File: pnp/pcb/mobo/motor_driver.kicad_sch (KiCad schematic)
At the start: 34 parts, among them M9 Stepper_Motor, U6 TMC2226-SA

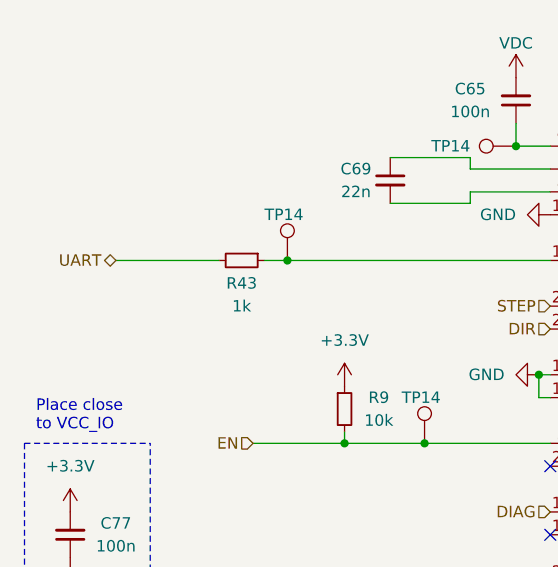
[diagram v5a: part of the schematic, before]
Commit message: Add notes to pending symbols
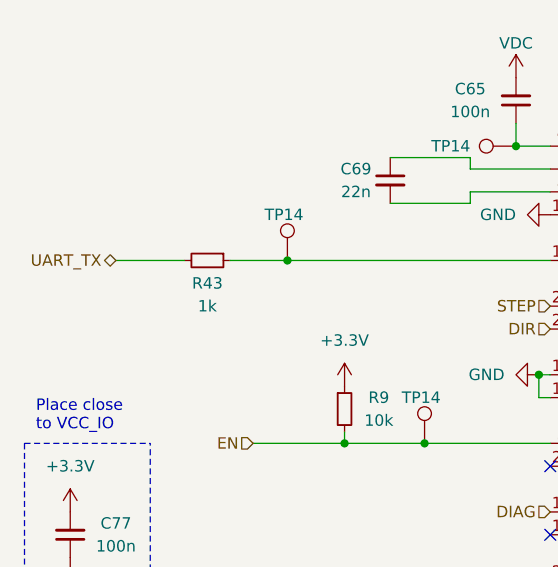
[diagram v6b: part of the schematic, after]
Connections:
- net UART renamed UART_TX
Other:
- moved on the sheet: R43
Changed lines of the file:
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@@
     (stroke (width 0) (type default))
   )
-  (wire (pts (xy 49.53 55.88) (xy 52.07 55.88))
+  (wire (pts (xy 45.72 55.88) (xy 52.07 55.88))
     (stroke (width 0) (type default))
   )
@@
     (stroke (width 0) (type default))
   )
-  (wire (pts (xy 33.02 55.88) (xy 44.45 55.88))
+  (wire (pts (xy 33.02 55.88) (xy 40.64 55.88))
     (stroke (width 0) (type default))
   )
@@
     (effects (font (size 1.27 1.27)) (justify right))
   )
-  (hierarchical_label "UART" (shape bidirectional) (at 33.02 55.88 180) (fields_autoplaced)
+  (hierarchical_label "UART_TX" (shape bidirectional) (at 33.02 55.88 180) (fields_autoplaced)
     (effects (font (size 1.27 1.27)) (justify right))
   )
@@
     )
   )
-  (symbol (lib_id "Device:R_Small") (at 46.99 55.88 270) (unit 1)
-    (in_bom yes) (on_board yes) (dnp no)
-    (property "Reference" "R43" (at 46.99 58.42 90)
-      (effects (font (size 1.27 1.27)))
-    )
-    (property "Value" "1k" (at 46.99 60.96 90)
-      (effects (font (size 1.27 1.27)))
-    )
-    (property "Footprint" "Resistor_SMD:R_0805_2012Metric" (at 46.99 54.102 90)
-      (effects (font (size 1.27 1.27)) hide)
-    )
-    (property "Datasheet" "" (at 46.99 55.88 0)
-      (effects (font (size 1.27 1.27)) hide)
-    )
-    (property "Digikey" "" (at 46.99 55.88 0)
-      (effects (font (size 1.27 1.27)) hide)
-    )
-    (property "JLCPCB" "C17513" (at 46.99 55.88 0)
-      (effects (font (size 1.27 1.27)) hide)
-    )
-    (property "LCSC" "C17513" (at 46.99 55.88 0)
-      (effects (font (size 1.27 1.27)) hide)
-    )
-    (property "Mouser" "" (at 46.99 55.88 0)
-      (effects (font (size 1.27 1.27)) hide)
-    )
-    (property "Notes" "" (at 46.99 55.88 0)
-      (effects (font (size 1.27 1.27)) hide)
-    )
+  (symbol (lib_id "Device:R_Small") (at 43.18 55.88 270) (unit 1)
+    (in_bom yes) (on_board yes) (dnp no)
+    (property "Reference" "R43" (at 43.18 58.42 90)
+      (effects (font (size 1.27 1.27)))
+    )
+    (property "Value" "1k" (at 43.18 60.96 90)
+      (effects (font (size 1.27 1.27)))
+    )
+    (property "Footprint" "Resistor_SMD:R_0805_2012Metric" (at 43.18 54.102 90)
+      (effects (font (size 1.27 1.27)) hide)
+    )
+    (property "Datasheet" "" (at 43.18 55.88 0)
+      (effects (font (size 1.27 1.27)) hide)
+    )
+    (property "Digikey" "" (at 43.18 55.88 0)
+      (effects (font (size 1.27 1.27)) hide)
+    )
+    (property "JLCPCB" "C17513" (at 43.18 55.88 0)
+      (effects (font (size 1.27 1.27)) hide)
+    )
+    (property "LCSC" "C17513" (at 43.18 55.88 0)
+      (effects (font (size 1.27 1.27)) hide)
+    )
+    (property "Mouser" "" (at 43.18 55.88 0)
+      (effects (font (size 1.27 1.27)) hide)
+    )
+    (property "Notes" "" (at 43.18 55.88 0)
+      (effects (font (size 1.27 1.27)) hide)
+    )

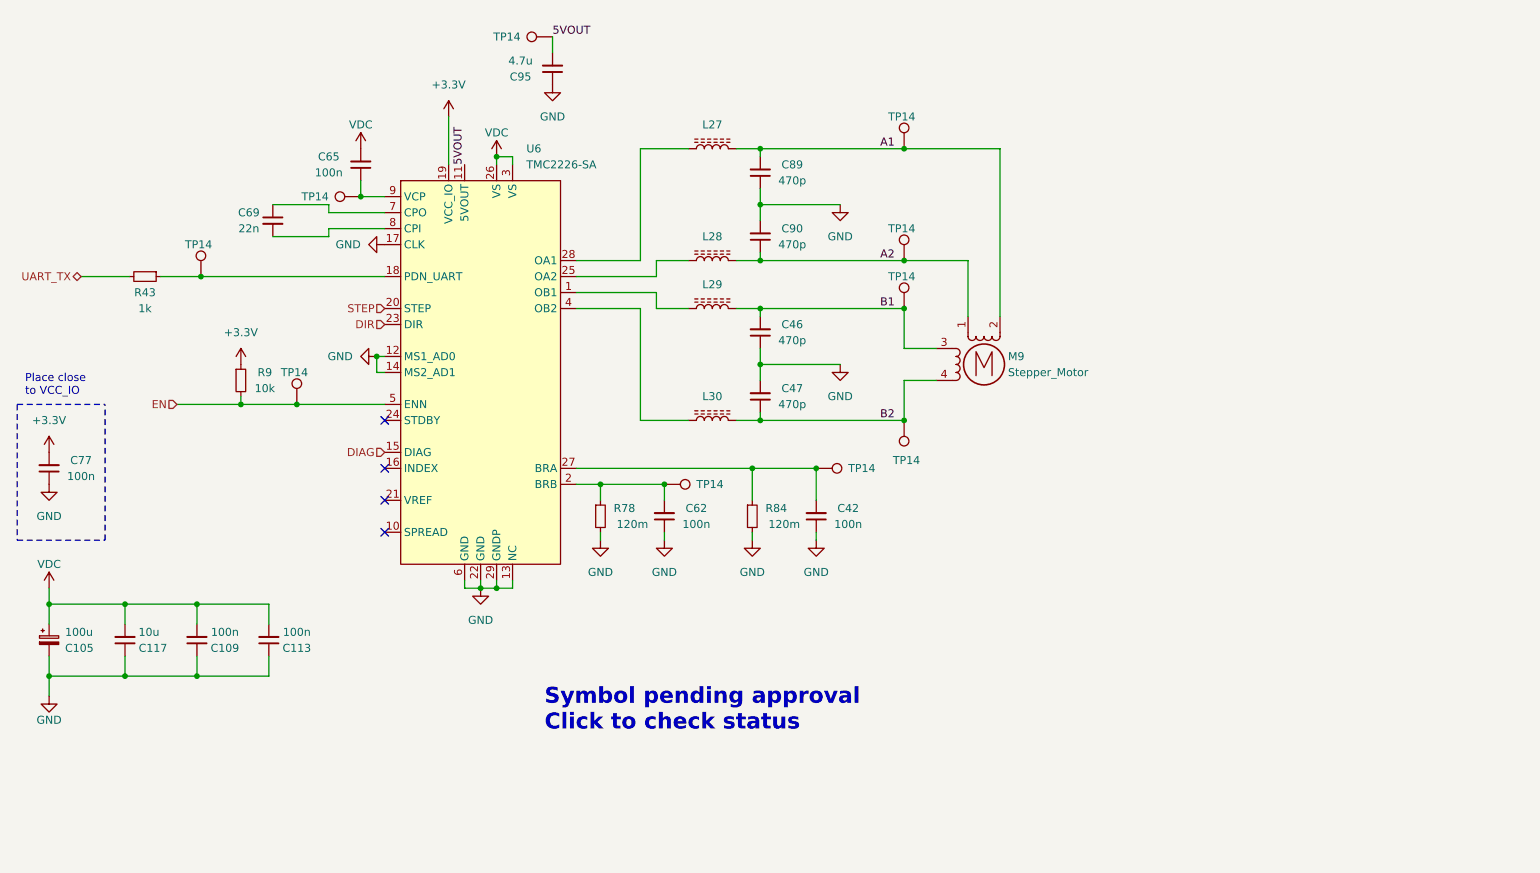
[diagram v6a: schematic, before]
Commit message: Schematic almost finished
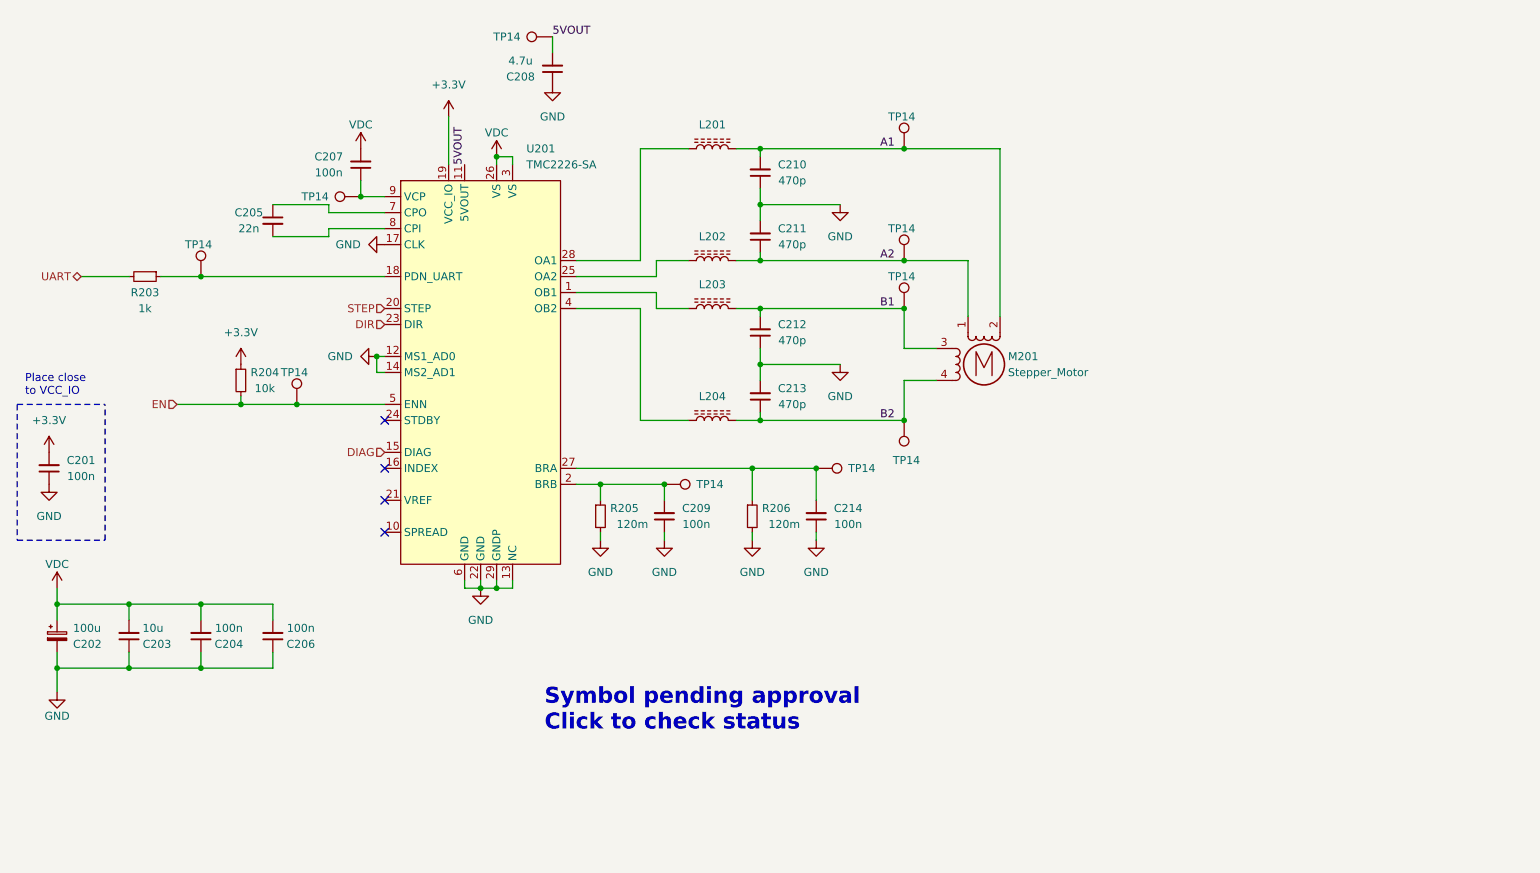
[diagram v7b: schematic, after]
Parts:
- U201: renamed from U6; footprint Package_SO:HTSSOP-28-1EP_4.4x9.7mm_P0.65mm_EP2.75x6.2mm_ThermalVias -> index:HTSSOP-28-1EP_4.4x9.7mm_P0.65mm_EP2.75x6.2mm_ThermalVias
- renumbered C77 to C201, C105 to C202, C117 to C203, C109 to C204, C69 to C205, C113 to C206, C65 to C207, C95 to C208, C62 to C209, C89 to C210, C90 to C211, C46 to C212, C47 to C213, C42 to C214, L27 to L201, L28 to L202, L29 to L203, L30 to L204, M9 to M201, R43 to R203, R9 to R204, R78 to R205, R84 to R206
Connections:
- net UART_TX renamed UART
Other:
- moved on the sheet: C202, C203, C204, C206

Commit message: Finished reverse polarity and inrush current circuits
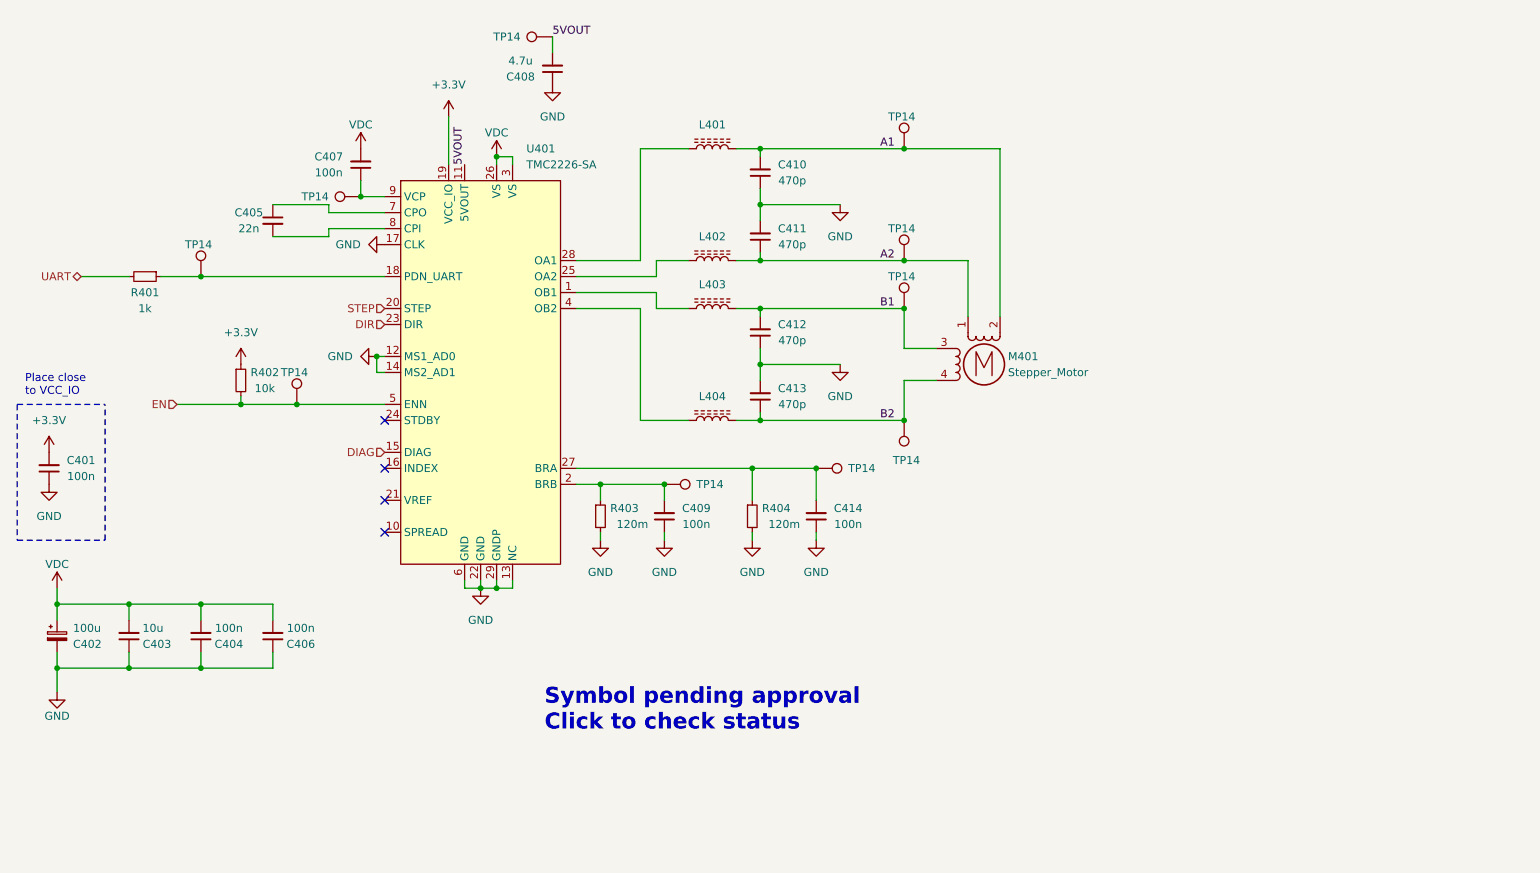
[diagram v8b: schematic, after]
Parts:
- renumbered C201 to C401, C202 to C402, C203 to C403, C204 to C404, C205 to C405, C206 to C406, C207 to C407, C208 to C408, C209 to C409, C210 to C410, C211 to C411, C212 to C412, C213 to C413, C214 to C414, L201 to L401, L202 to L402, L203 to L403, L204 to L404, M201 to M401, R203 to R401, R204 to R402, R205 to R403, R206 to R404, U201 to U401
